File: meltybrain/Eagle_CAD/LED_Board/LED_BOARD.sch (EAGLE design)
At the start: 17 parts, among them J1 SM04B-SRSS-TB(LF)(SN)

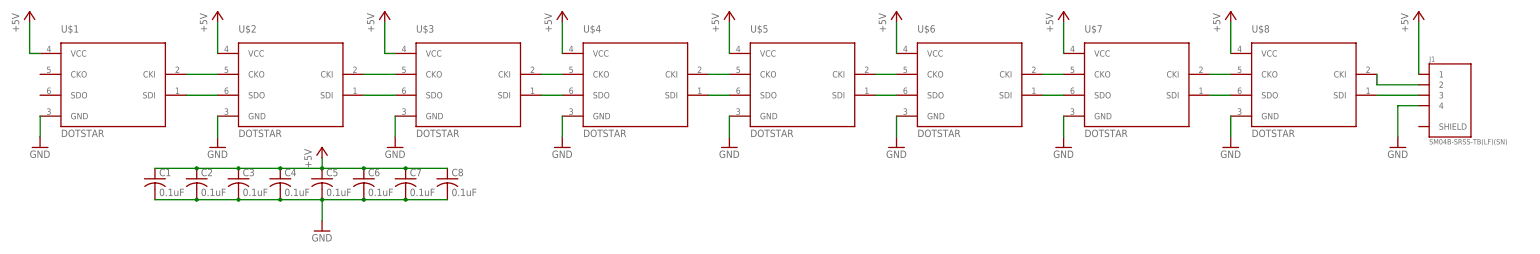
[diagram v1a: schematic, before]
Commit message: Changes to led board
adjusted screw holes
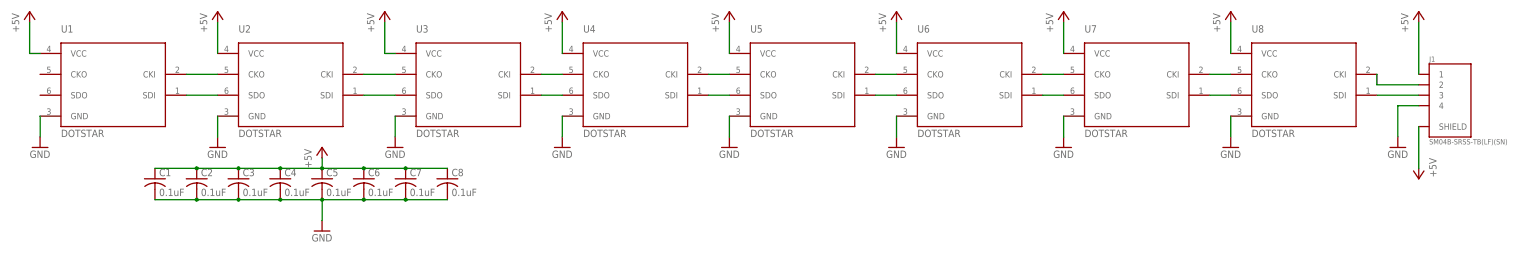
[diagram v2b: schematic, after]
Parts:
- renumbered U$1 to U1, U$2 to U2, U$3 to U3, U$4 to U4, U$5 to U5, U$6 to U6, U$7 to U7, U$8 to U8
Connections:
- net +5V: now also J1.SHIELD

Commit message: Changes to LED board
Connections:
- net +5V: no longer J1.SHIELD
- net GND: now also J1.SHIELD
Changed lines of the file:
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@@
 <part name="P+10" library="supply1" library_urn="urn:adsk.eagle:library:371" deviceset="+5V" device=""/>
 <part name="GND10" library="supply1" library_urn="urn:adsk.eagle:library:371" deviceset="GND" device=""/>
-<part name="P+11" library="supply1" library_urn="urn:adsk.eagle:library:371" deviceset="+5V" device=""/>
+<part name="GND11" library="supply1" library_urn="urn:adsk.eagle:library:371" deviceset="GND" device=""/>
 </parts>
 <sheets>
@@
 <attribute name="VALUE" x="368.3" y="35.56" size="1.778" layer="96"/>
 </instance>
-<instance part="P+11" gate="1" x="375.92" y="30.48" smashed="yes" rot="R180">
-<attribute name="VALUE" x="378.46" y="35.56" size="1.778" layer="96" rot="R270"/>
+<instance part="GND11" gate="1" x="375.92" y="30.48" smashed="yes">
+<attribute name="VALUE" x="373.38" y="27.94" size="1.778" layer="96"/>
 </instance>
 </instances>
@@
 <wire x1="375.92" y1="55.88" x2="375.92" y2="68.58" width="0.1524" layer="91"/>
 </segment>
-<segment>
-<pinref part="J1" gate="G$2" pin="SHIELD"/>
-<pinref part="P+11" gate="1" pin="+5V"/>
-<wire x1="375.92" y1="43.18" x2="375.92" y2="33.02" width="0.1524" layer="91"/>
-</segment>
 </net>
 <net name="GND" class="0">
@@
 <wire x1="370.84" y1="48.26" x2="370.84" y2="40.64" width="0.1524" layer="91"/>
 </segment>
-</net>
+<segment>
+<pinref part="J1" gate="G$2" pin="SHIELD"/>
+<wire x1="375.92" y1="43.18" x2="375.92" y2="33.02" width="0.1524" layer="91"/>
+<pinref part="GND11" gate="1" pin="GND"/>
+</segment>
+</net>
